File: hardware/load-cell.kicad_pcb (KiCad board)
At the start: 2 copper layers, 30 x 30 mm, 21 parts, among them P1 CON-SENSOR, P2 AKL_5_2, P3 AKL_5_2, U1 M24C64, U2 HX711, U3 DRILL, U4 DRILL, U5 DRILL, U6 DRILL

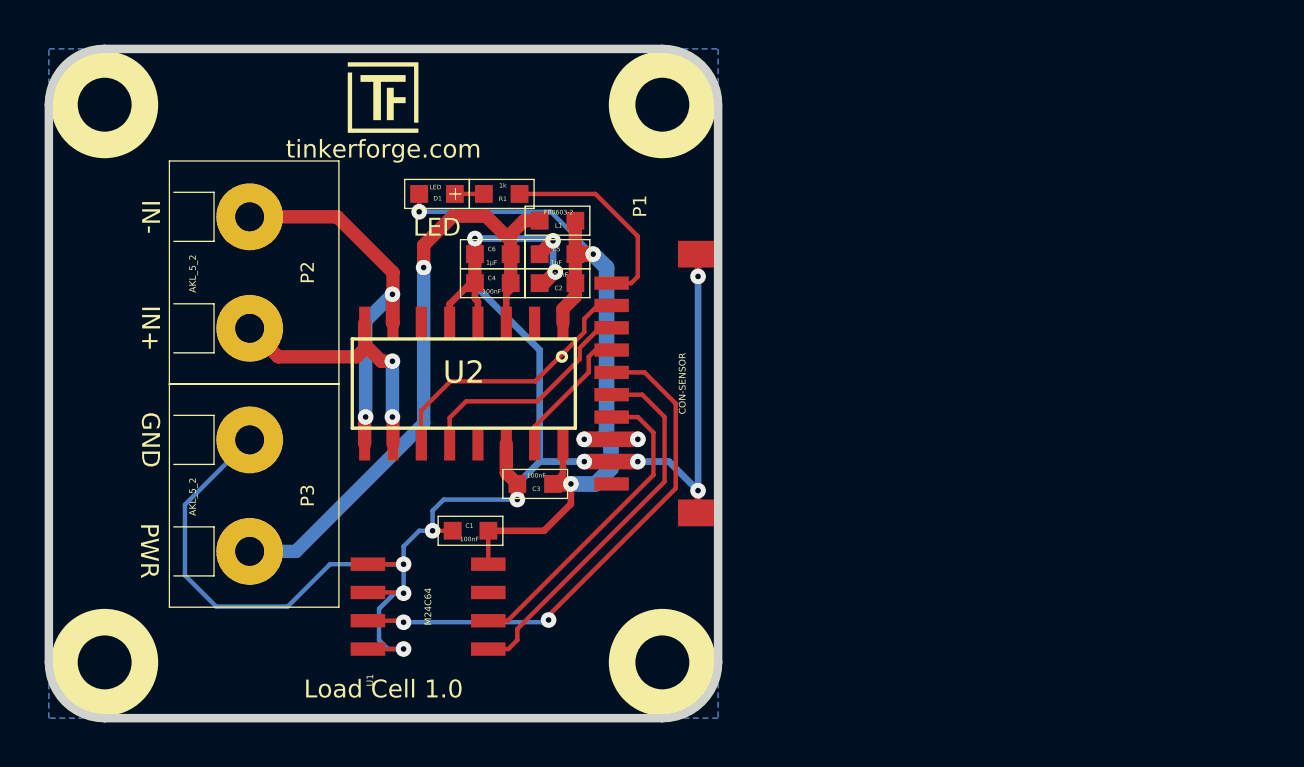
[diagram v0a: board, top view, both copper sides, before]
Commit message: add 5v boost regulator, routing not finished
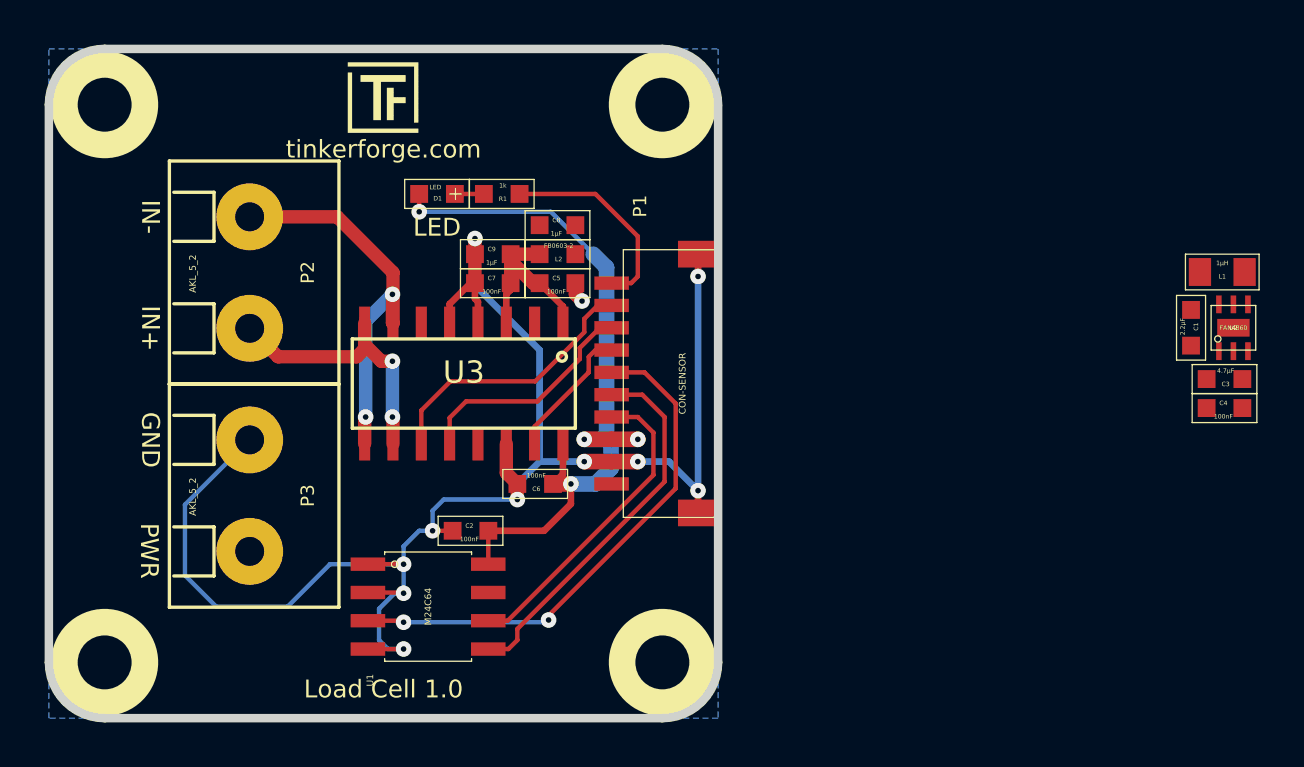
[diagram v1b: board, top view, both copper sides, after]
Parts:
- added C7: 100nF, kicad-libraries:0603, F.Cu at (157.9, 95.6)
- added C8: 1µF, kicad-libraries:0603, F.Cu at (160.8, 93.0)
- added C9: 1µF, kicad-libraries:0603, F.Cu at (157.9, 94.3)
- added L2: FB0603-2, kicad-libraries:0603, F.Cu at (160.8, 94.3)
- added U7: DRILL, kicad-libraries:DRILL_NP, F.Cu at (165.6, 87.6)
- C1: value 100nF -> 2.2µF; footprint 0603 -> kicad-libraries:0603
- C2, C4, R1: footprint 0603 -> kicad-libraries:0603
- C3: value 100nF -> 4.7µF; footprint 0603 -> kicad-libraries:0603
- C5, C6: value 1µF -> 100nF; footprint 0603 -> kicad-libraries:0603
- D1: footprint D0603 -> kicad-libraries:D0603
- L1: value FB0603-2 -> 1µH; footprint 0603 -> kicad-libraries:0805
- P1: footprint CON-SENSOR -> kicad-libraries:CON-SENSOR
- P2, P3: footprint AKL_5_2 -> kicad-libraries:AKL_5_2
- U1: footprint SOIC8 -> kicad-libraries:SOIC8
- U2: value HX711 -> FAN4860; footprint kicad-libraries:SOP16L -> kicad-libraries:UMLP_22
- U3: value DRILL -> HX711; footprint DRILL_NP -> kicad-libraries:SOP16L
- U4, U5, U6: footprint DRILL_NP -> kicad-libraries:DRILL_NP
- moved U2 34.6 mm to (191.2, 97.6)
- moved C1 33.6 mm to (189.2, 97.6), turned to 90 degrees
- moved C4 33.3 mm to (190.8, 101.2)
- moved C3 31.3 mm to (190.8, 99.9)
- moved L1 29.9 mm to (190.7, 95.1)
- moved U3 15.3 mm to (156.7, 100.1), turned to 180 degrees
- moved C2 11.8 mm to (156.9, 106.7), turned to 180 degrees
- moved C6 10.5 mm to (159.8, 104.6), turned to 0 degrees
- moved C5 1.30 mm to (160.8, 95.6)
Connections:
- C1 pad 1: 3V3 -> AGND
- C1 pad 2: AGND -> 3V3
- C2 pad 1: AGND -> 3V3
- C2 pad 2: 3V3 -> AGND
- C3 pad 2: 3V3 -> +5V
- C4 pad 1: +3.3VP -> +5V
- C5 pad 1: 3V3 -> AGND
- C5 pad 2: AGND -> +5VA
- C6 pad 1: +3.3VP -> AGND
- C6 pad 2: AGND -> 3V3
- L1 pad 1: +3.3VP -> Net-(L1-Pad1)
- P2 pad 1: Net-(P2-Pad1) -> (no net)
- P2 pad 2: Net-(P2-Pad2) -> AGND
- P3 pad 1: +3.3VP -> Net-(P3-Pad1)
- P3 pad 2: AGND -> Net-(P3-Pad2)
- U2 pad 1: 3V3 -> AGND
- U2 pad 2: (no net) -> +5V
- U2 pad 3: +3.3VP -> +5V
- U2 pad 4: AGND -> 3V3
- U2 pad 5: AGND -> Net-(L1-Pad1)
- U2 pad 6: (no net) -> 3V3
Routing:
- net +3.3VP: track 28.8 -> 0.00 mm, vias 1 -> 0
- net Net-(P2-Pad2): track 18.3 -> 0.00 mm, vias 2 -> 0
- net Net-(P3-Pad2): track 0.00 -> 14.9 mm, vias 0 -> 2
- net Net-(P3-Pad1): track 0.00 -> 12.2 mm, vias 0 -> 2
- net Net-(P2-Pad1): track 12.2 -> 0.00 mm, vias 2 -> 0
- net +5VA: track 0.00 -> 9.08 mm
- net 3V3: track 40.3 -> 34.2 mm, vias 5 -> 4
- net AGND: track 85.0 -> 82.6 mm, vias 12 -> 11

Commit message: routing finished
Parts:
- removed C9: 1µF, kicad-libraries:0603
- moved U2 32.2 mm to (160.1, 89.3)
- moved L1 32.0 mm to (159.7, 86.7), turned to 180 degrees
- moved C1 32.0 mm to (158.4, 89.2)
- moved C3 31.0 mm to (160.8, 91.7)
- moved C4 31.0 mm to (160.8, 93.0)
- moved D1 17.4 mm to (162.0, 107.7)
- moved R1 17.4 mm to (164.9, 107.7)
- moved C8 3.18 mm to (157.9, 94.3)
- moved U1 2.10 mm to (155.1, 108.0)
- moved C2 2.10 mm to (156.9, 104.6), turned to 0 degrees
- moved VAL 0.80 mm to (150.8, 100.1)
- moved G*** 0.28 mm to (151.4, 85.4)
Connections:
- C8 pad 1: +5V -> +5VA
- P2 pad 1: (no net) -> Net-(P2-Pad1)
- P2 pad 2: AGND -> Net-(P2-Pad2)
- P3 pad 1: Net-(P3-Pad1) -> (no net)
- P3 pad 2: Net-(P3-Pad2) -> AGND
- U3 pad 10: Net-(P3-Pad1) -> Net-(P2-Pad1)
- U3 pad 7: Net-(P3-Pad2) -> Net-(P2-Pad2)
- U3 pad 8: Net-(P3-Pad1) -> Net-(P2-Pad1)
- U3 pad 9: Net-(P3-Pad2) -> Net-(P2-Pad2)
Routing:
- net Net-(P2-Pad2): track 0.00 -> 18.3 mm, vias 0 -> 2
- net AGND: track 82.6 -> 98.7 mm, vias 11 -> 13
- net Net-(P3-Pad2): track 14.9 -> 0.00 mm, vias 2 -> 0
- net Net-(P2-Pad1): track 0.00 -> 12.2 mm, vias 0 -> 2
- net Net-(P3-Pad1): track 12.2 -> 0.00 mm, vias 2 -> 0
- net 3V3: track 34.2 -> 46.4 mm, vias 4 -> 6
- net +5V: track 0.00 -> 5.64 mm
- net Net-(P1-Pad10): track 9.19 -> 14.2 mm
- net Net-(L1-Pad1): track 0.00 -> 1.83 mm
- net SDA: track 17.0 -> 15.6 mm, vias 0 -> 2
- net SCL: track 14.2 -> 13.3 mm, vias 0 -> 2

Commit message: add fiducials
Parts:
- added Fiducial_Mark: VAL**, kicad-libraries:Fiducial_Mark, F.Cu at (145.6, 86.6)
- added Fiducial_Mark: VAL**, kicad-libraries:Fiducial_Mark, F.Cu at (160.6, 113.6)

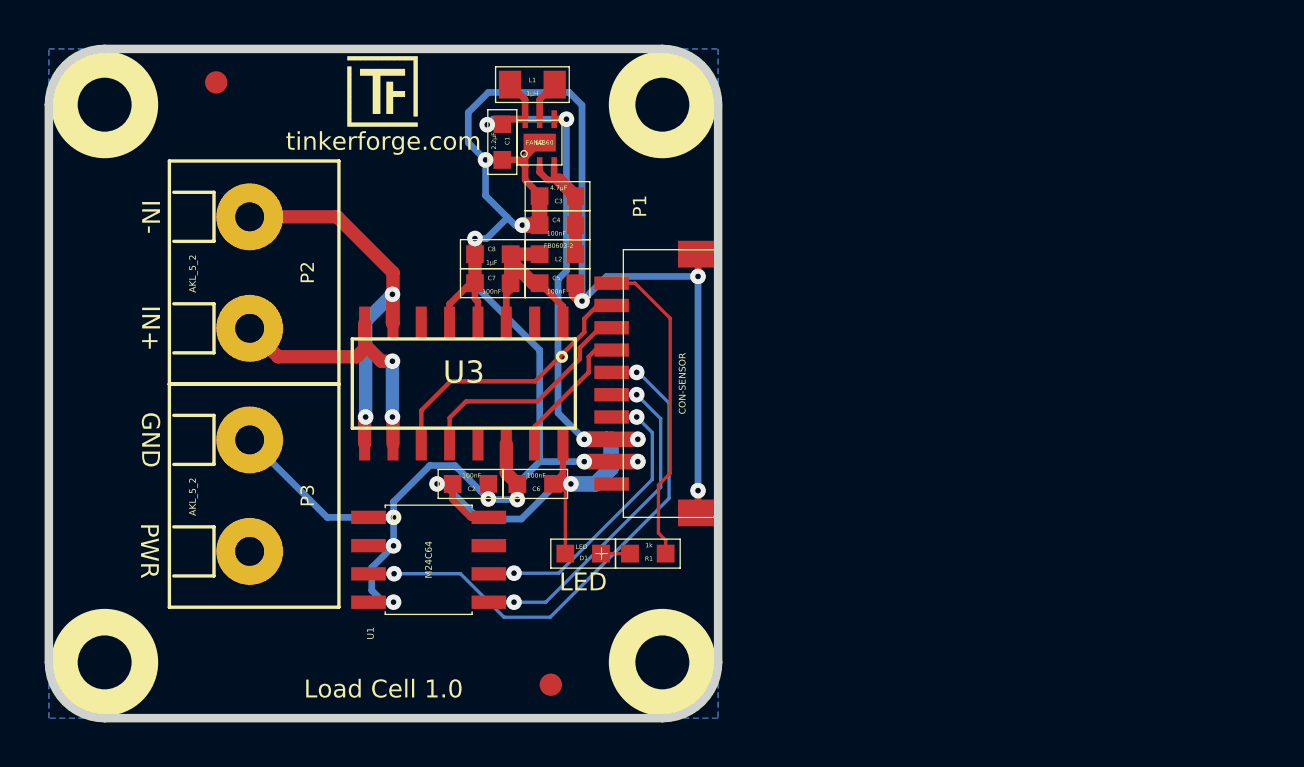
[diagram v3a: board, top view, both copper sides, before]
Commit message: change port description, fix routing
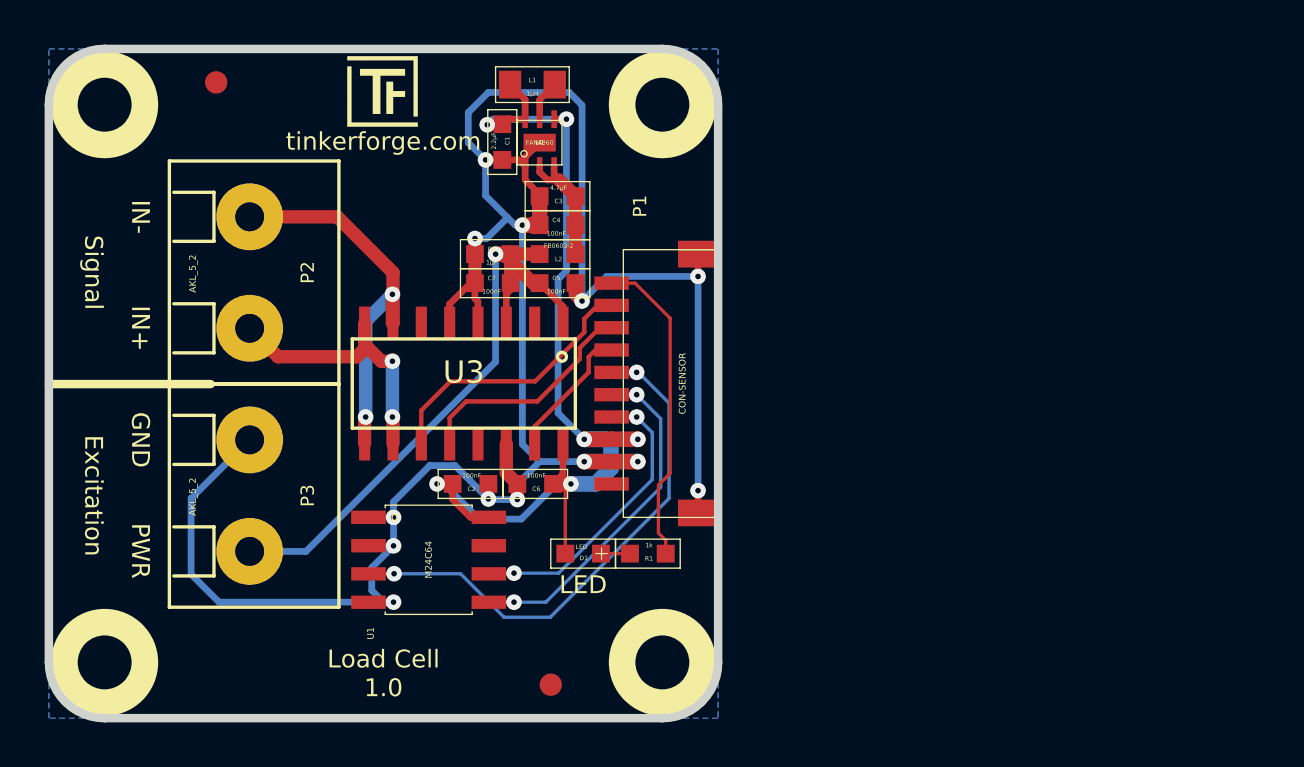
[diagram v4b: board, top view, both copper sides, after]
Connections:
- P3 pad 1: (no net) -> +5VA
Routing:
- net +5VA: track 9.08 -> 29.1 mm, vias 0 -> 1
- net AGND: track 98.7 -> 107.2 mm
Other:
- board text added: "Excitation"
- board text added: "Signal"
